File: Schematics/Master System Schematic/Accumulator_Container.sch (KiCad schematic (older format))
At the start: 20 parts, among them J10 Main TS Connector, J11 TSAL Connector, J8 Shutdown/MC Control Connector, J9 TSMP/IMD Connector, K10 SPST-NO (Precharge Control), K11 SPST-NC (Discharge), K12 SPST-NO (AIR Control), K7 SPST-NO (Precharge), K8 SPST-NO (AIR), K9 SPST-NO (AIR), U14 OrionCurrentSens

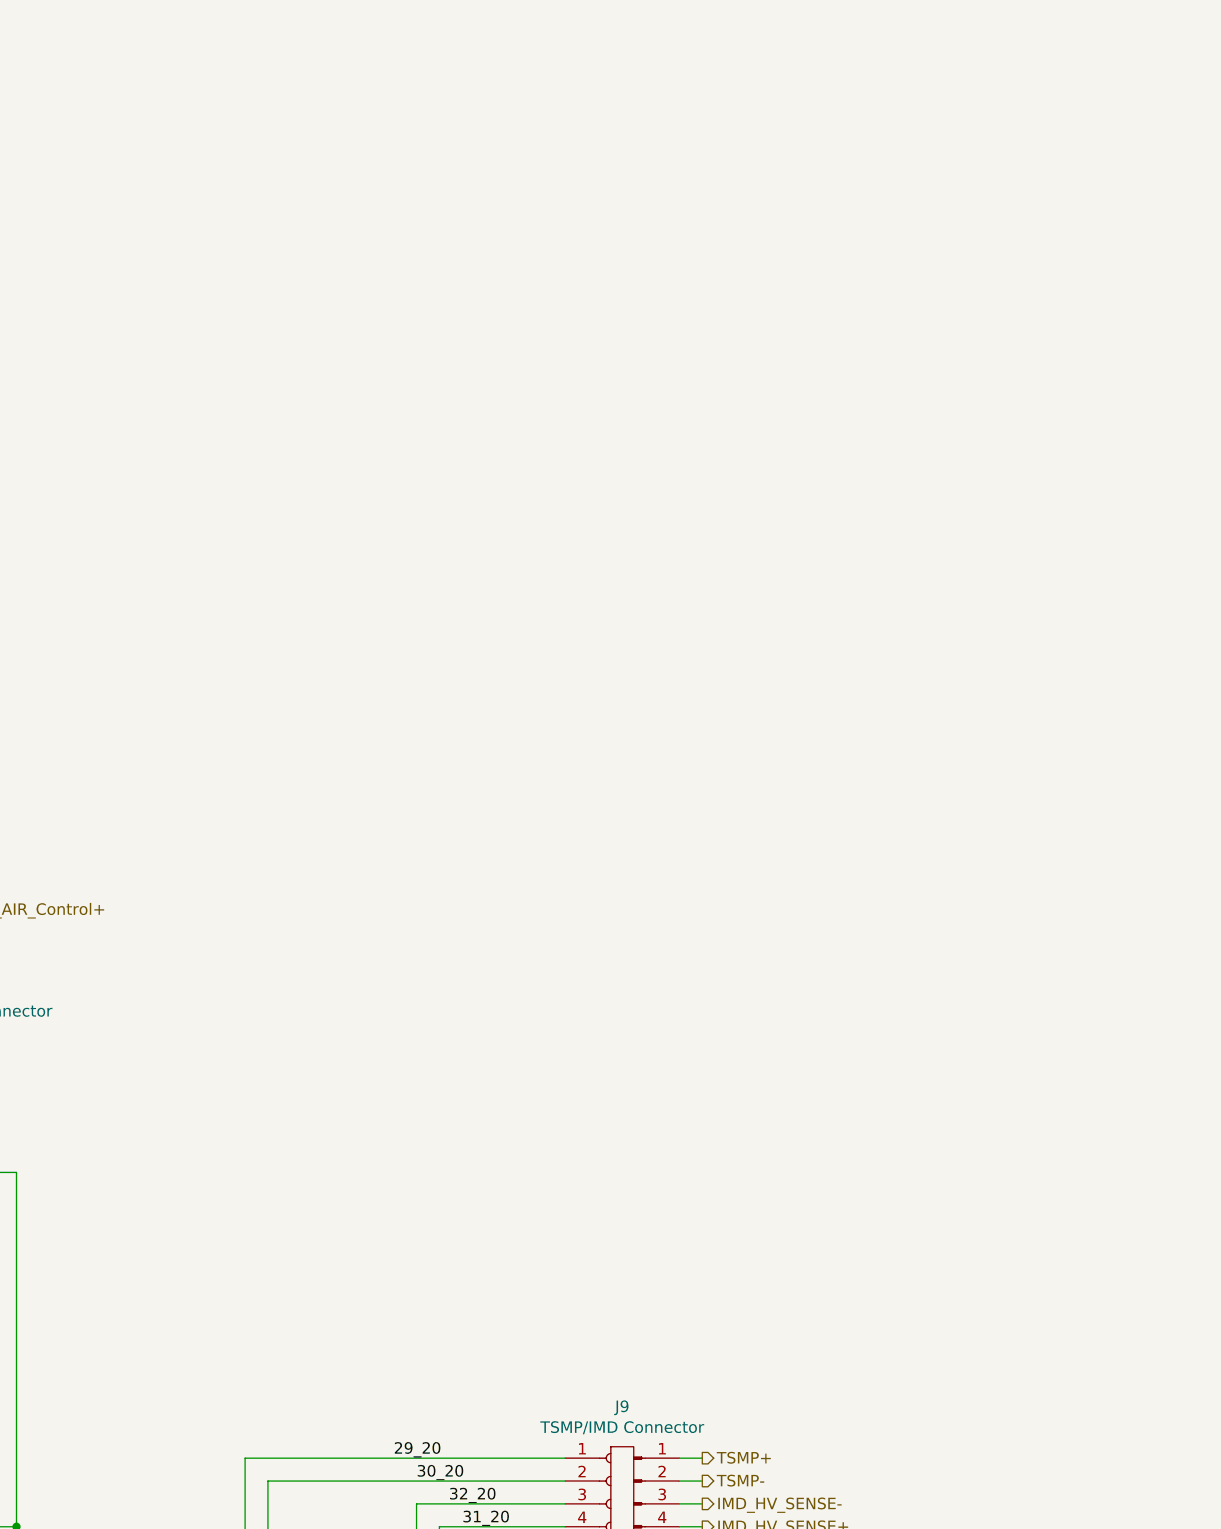
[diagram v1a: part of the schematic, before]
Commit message: Moved Thermistor Exp and MC out of BMS container
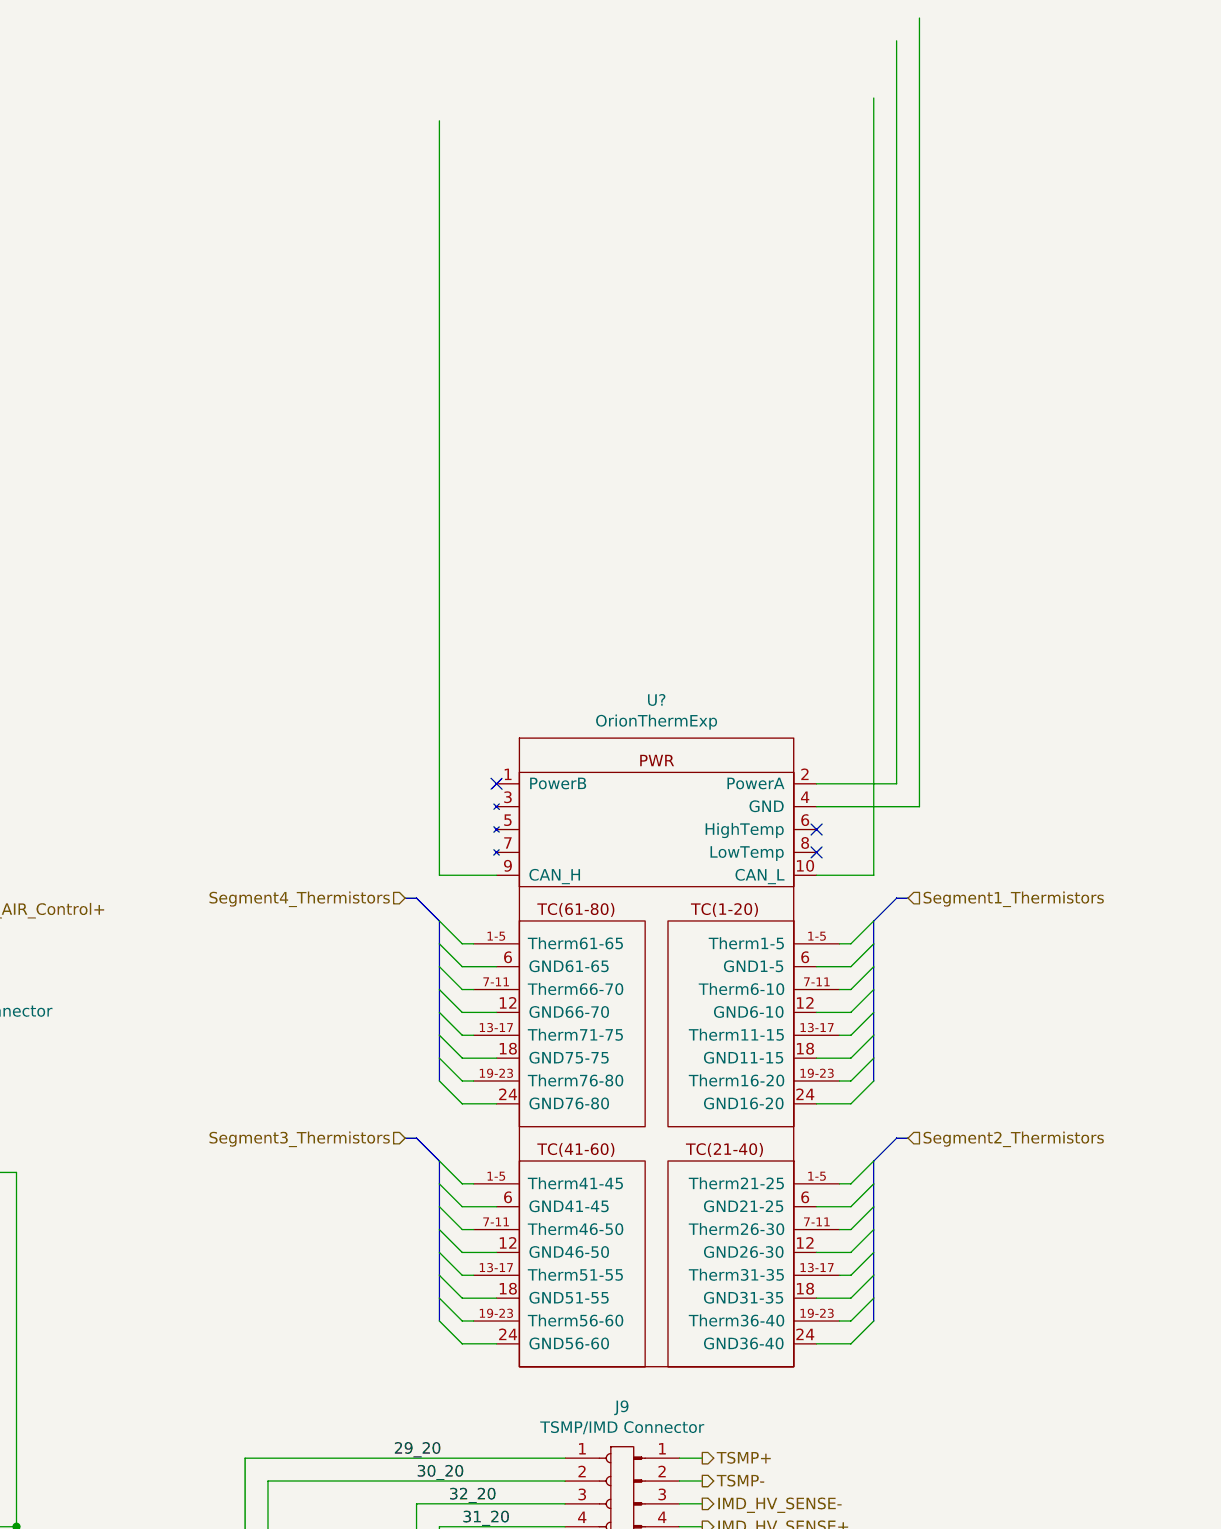
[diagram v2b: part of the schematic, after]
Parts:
- added U?: OrionThermExp, symbol NER:OrionThermExp
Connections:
- no-connect marks 0 -> 3
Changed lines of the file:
@@
 Wire Wire Line
 	9950 600  9950 1050
+Text HLabel 12900 1900 0    50   Input ~ 0
+Segment3_Thermistors
+Text HLabel 15100 850  2    50   Input ~ 0
+Segment1_Thermistors
+Entry Wire Line
+	14850 1750 14950 1650
+Entry Wire Line
+	14850 1650 14950 1550
+Entry Wire Line
+	14850 1550 14950 1450
+Entry Wire Line
+	14850 1450 14950 1350
+Entry Wire Line
+	14850 1350 14950 1250
+Entry Wire Line
+	14850 1250 14950 1150
+Entry Wire Line
+	14850 1150 14950 1050
+Entry Wire Line
+	14850 1050 14950 950
+Entry Bus Bus
+	14950 950  15050 850
+Wire Bus Line
+	15050 850  15100 850
+Entry Wire Line
+	13150 1650 13050 1550
+Entry Wire Line
+	13150 1550 13050 1450
+Entry Wire Line
+	13150 1450 13050 1350
+Entry Wire Line
+	13150 1350 13050 1250
+Entry Wire Line
+	13150 1250 13050 1150
+Entry Wire Line
+	13150 1150 13050 1050
+Entry Wire Line
+	13150 1050 13050 950
+Entry Bus Bus
+	13050 950  12950 850
+Wire Bus Line
+	12950 850  12900 850
+Entry Wire Line
+	13150 2800 13050 2700
+Entry Wire Line
+	13150 2700 13050 2600
+Entry Wire Line
+	13150 2600 13050 2500
+Entry Wire Line
+	13150 2500 13050 2400
+Entry Wire Line
+	13150 2400 13050 2300
+Entry Wire Line
+	13150 2300 13050 2200
+Entry Wire Line
+	13150 2200 13050 2100
+Entry Wire Line
+	13150 2100 13050 2000
+Entry Bus Bus
+	13050 2000 12950 1900
+Wire Bus Line
+	12950 1900 12900 1900
+Entry Wire Line
+	14850 2100 14950 2000
+Entry Wire Line
+	14850 2200 14950 2100
+Entry Wire Line
+	14850 2300 14950 2200
+Entry Wire Line
+	14850 2400 14950 2300
+Entry Wire Line
+	14850 2500 14950 2400
+Entry Wire Line
+	14850 2600 14950 2500
+Entry Wire Line
+	14850 2700 14950 2600
+Entry Wire Line
+	14850 2800 14950 2700
+Text HLabel 15100 1900 2    50   Input ~ 0
+Segment2_Thermistors
+Wire Bus Line
+	15050 1900 15100 1900
+Entry Bus Bus
+	14950 2000 15050 1900
+Text HLabel 12900 850  0    50   Input ~ 0
+Segment4_Thermistors
+Entry Wire Line
+	13150 1750 13050 1650
+Wire Wire Line
+	13150 1050 13200 1050
+Wire Wire Line
+	13150 1150 13300 1150
+Wire Wire Line
+	13150 1250 13200 1250
+Wire Wire Line
+	13150 1350 13300 1350
+Wire Wire Line
+	13200 1450 13150 1450
+Wire Wire Line
+	13150 1550 13300 1550
+Wire Wire Line
+	13150 1650 13200 1650
+Wire Wire Line
+	13150 1750 13300 1750
+Wire Wire Line
+	13200 2100 13150 2100
+Wire Wire Line
+	13150 2200 13300 2200
+Wire Wire Line
+	13150 2300 13200 2300
+Wire Wire Line
+	13150 2400 13300 2400
+Wire Wire Line
+	13150 2500 13200 2500
+Wire Wire Line
+	13150 2600 13300 2600
+Wire Wire Line
+	13150 2700 13200 2700
+Wire Wire Line
+	13150 2800 13300 2800
+Wire Wire Line
+	14850 2100 14800 2100
+Wire Wire Line
+	14850 2200 14700 2200
+Wire Wire Line
+	14850 2300 14800 2300
+Wire Wire Line
+	14700 2400 14850 2400
+Wire Wire Line
+	14800 2500 14850 2500
+Wire Wire Line
+	14700 2600 14850 2600
+Wire Wire Line
+	14850 2700 14800 2700
+Wire Wire Line
+	14700 2800 14850 2800
+Wire Wire Line
+	14700 1750 14850 1750
+Wire Wire Line
+	14850 1650 14800 1650
+Wire Wire Line
+	14850 1550 14700 1550
+Wire Wire Line
+	14850 1450 14800 1450
+Wire Wire Line
+	14850 1350 14700 1350
+Wire Wire Line
+	14850 1250 14800 1250
+Wire Wire Line
+	14850 1150 14700 1150
+Wire Wire Line
+	14800 1050 14850 1050
+NoConn ~ 14700 550
+NoConn ~ 14700 650
+NoConn ~ 13300 350
+$Comp
+L NER:OrionThermExp U?
+U 1 1 5FB81724
+P 14000 150
+F 0 "U?" H 14000 315 50  0000 C CNN
+F 1 "OrionThermExp" H 14000 224 50  0000 C CNN
+F 2 "" H 14000 50  50  0001 C CNN
+F 3 "" H 14000 50  50  0001 C CNN
+	1    14000 150
+	1    0    0    -1
+$EndComp
+Wire Wire Line
+	14700 750  14950 750
+Wire Wire Line
+	13050 750  13300 750
+Wire Wire Line
+	15150 450  14700 450
+Wire Wire Line
+	14700 350  15050 350
+Wire Wire Line
+	13050 -2550 13050 750
+Wire Wire Line
+	14950 -2650 14950 750
+Wire Wire Line
+	15050 -2900 15050 350
+Wire Wire Line
+	15150 -3000 15150 450
 Wire Bus Line
 	5950 9200 5950 9800
@@
 Wire Bus Line
 	13900 5350 15900 5350
+Wire Bus Line
+	14950 950  14950 1650
+Wire Bus Line
+	13050 950  13050 1650
+Wire Bus Line
+	13050 2000 13050 2700
+Wire Bus Line
+	14950 2000 14950 2700
 $EndSCHEMATC

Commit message: added thermistor expansion to Accumulator container
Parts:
- gave numbers to parts that had none: 1
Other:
- note added: "All leave the accumulator container via cord grips"
- note added: "Current sense line will be fed from the accumulator to the BMS via its own connector"
- note removed: "Current sense line will be fed from the accumulator to the BMS via the thermistor connectors, and then split back out within the BMS container. May also be done via a separate connector. TBD"
- moved on the sheet: F5, F6, F7, F8, F9, J10, J11, J8, J9, K10, K11, K12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

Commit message: fixed therm boards
fixed therm board implementation
beginning accumulator redraw
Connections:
- wire segments 372 -> 436
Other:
- moved on the sheet: U7

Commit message: roughly spread out accumulator components, updated therms boards
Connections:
- wire segments 436 -> 438
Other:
- note removed: "Current sense line will be fed from the accumulator to the BMS via its own connector"
- moved on the sheet: F5, F6, F7, F8, F9, J10, J11, J8, J9, K10, K11, K12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

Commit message: Master cleanup
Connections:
- net 1_2: now also F6.1; no longer F6.2
- net TSAL_Circuit/VBATT-: now also F6.2; no longer F6.1
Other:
- moved on the sheet: F6, K11, R3
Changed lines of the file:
@@
 L Relay:MSxx-1Bxx-75 K11
 U 1 1 5E637554
-P 14300 8700
-F 0 "K11" V 13733 8700 50  0000 C CNN
-F 1 "SPST-NC (Discharge)" V 13824 8700 50  0000 C CNN
-F 2 "Relay_THT:Relay_SPST_StandexMeder_MS_Form1AB" H 14650 8650 50  0001 L CNN
-F 3 "https://standexelectronics.com/de/produkte/ms-reed-relais/" H 14300 8700 50  0001 C CNN
-	1    14300 8700
+P 14500 10450
+F 0 "K11" V 13933 10450 50  0000 C CNN
+F 1 "SPST-NC (Discharge)" V 14024 10450 50  0000 C CNN
+F 2 "Relay_THT:Relay_SPST_StandexMeder_MS_Form1AB" H 14850 10400 50  0001 L CNN
+F 3 "https://standexelectronics.com/de/produkte/ms-reed-relais/" H 14500 10450 50  0001 C CNN
+	1    14500 10450
 	0    1    1    0
 $EndComp
@@
 Connection ~ 12850 7500
 Wire Wire Line
-	12850 7500 12850 8500
-Wire Wire Line
-	14000 8500 12850 8500
+	14200 10250 12850 10250
 Wire Wire Line
 	13750 6500 13850 6500
-Wire Wire Line
-	13950 8900 14000 8900
 $Comp
 L Device:R R3
 U 1 1 5F158D54
-P 15950 8300
-F 0 "R3" H 15750 8350 50  0000 L CNN
-F 1 "3.3k" H 15700 8250 50  0000 L CNN
-F 2 "" V 15880 8300 50  0001 C CNN
-F 3 "~" H 15950 8300 50  0001 C CNN
-	1    15950 8300
+P 15950 9250
+F 0 "R3" H 15750 9300 50  0000 L CNN
+F 1 "3.3k" H 15700 9200 50  0000 L CNN
+F 2 "" V 15880 9250 50  0001 C CNN
+F 3 "~" H 15950 9250 50  0001 C CNN
+	1    15950 9250
 	1    0    0    -1
 $EndComp
@@
 Text Label 15450 4400 0    50   ~ 0
 26_20
-Text Label 14800 8900 0    50   ~ 0
+Text Label 15000 10650 0    50   ~ 0
 13_2
 Text Label 13850 4250 2    50   ~ 0
@@
 	15100 3150 15200 3150
 Wire Wire Line
-	14600 8500 15450 8500
+	14800 10250 15450 10250
 Wire Wire Line
 	14250 3900 15200 3900
@@
 	15950 7900 16450 7900
 Wire Wire Line
-	15950 8150 15950 7900
-Wire Wire Line
-	15950 8450 15950 8900
-Wire Wire Line
-	14600 8900 15950 8900
+	15950 9100 15950 7900
+Wire Wire Line
+	14800 10650 15950 10650
 $Comp
 L NER:2-Pos_Generic J10
@@
 Wire Wire Line
 	2350 2200 2650 2200
-Wire Wire Line
-	11750 13850 13150 13850
-Wire Wire Line
-	11750 14300 11750 14400
 $Comp
 L Device:Fuse F6
 U 1 1 5FC95B82
-P 11750 14150
-F 0 "F6" H 11691 14104 50  0000 R CNN
-F 1 "Fuse" H 11691 14195 50  0000 R CNN
-F 2 "" V 11680 14150 50  0001 C CNN
-F 3 "~" H 11750 14150 50  0001 C CNN
-	1    11750 14150
+P 11850 13450
+F 0 "F6" H 11791 13404 50  0000 R CNN
+F 1 "Fuse" H 11791 13495 50  0000 R CNN
+F 2 "" V 11780 13450 50  0001 C CNN
+F 3 "~" H 11850 13450 50  0001 C CNN
+	1    11850 13450
 	1    0    0    1
 $EndComp
-Wire Wire Line
-	17700 14400 11750 14400
-Wire Wire Line
-	17600 14300 11850 14300
 Wire Wire Line
 	16550 8350 16550 13850
@@
 $EndComp
 Wire Wire Line
-	5250 13850 11750 13850
-Connection ~ 11750 13850
-Wire Wire Line
-	11750 13850 11750 14000
+	11850 11950 11850 13300
 Wire Wire Line
 	5250 13750 6100 13750
 Wire Wire Line
-	11850 7450 11850 14300
+	11850 7450 11850 11850
 Connection ~ 16550 8350
 Wire Wire Line
@@
 	17300 7900 17850 7900
 Wire Wire Line
-	17600 6350 17600 14300
-Wire Wire Line
-	17700 14400 17700 6450
-Connection ~ 12850 8500
-Wire Wire Line
-	12850 8500 12850 13450
-Wire Wire Line
-	15450 8500 15450 13450
-Wire Wire Line
-	13750 13850 13950 13850
-Wire Wire Line
-	13950 13850 16550 13850
-Connection ~ 13950 13850
-Wire Wire Line
-	13950 8900 13950 13850
+	17600 6350 17600 11850
 Wire Wire Line
 	13750 6900 15950 6900
-Wire Wire Line
-	15450 3900 15450 8500
 Connection ~ 15450 3900
-Connection ~ 15450 8500
 Wire Wire Line
 	14400 3550 14400 7500
@@
 	17100 15000 19650 15000
 Wire Bus Line
-	20150 7250 20150 12000
+	20700 7250 20700 12000
 Wire Bus Line
 	19250 13700 19650 13700
@@
 	20850 750  20850 12150
 Wire Bus Line
-	19100 12000 20150 12000
+	19100 12000 20700 12000
+Wire Bus Line
+	19250 12150 20850 12150
+Wire Wire Line
+	13750 13850 14000 13850
+Connection ~ 12850 10250
+Wire Wire Line
+	12850 10250 12850 13450
+Connection ~ 15450 10250
+Wire Wire Line
+	15450 10250 15450 13450
+Wire Wire Line
+	12850 7500 12850 10250
+Wire Wire Line
+	15450 3900 15450 10250
+Wire Wire Line
+	14200 10650 14000 10650
+Wire Wire Line
+	14000 10650 14000 13850
+Connection ~ 14000 13850
+Wire Wire Line
+	14000 13850 16550 13850
+Wire Wire Line
+	15950 9400 15950 10650
+Wire Wire Line
+	17700 11950 17700 6450
+Wire Wire Line
+	5250 13850 11850 13850
+Wire Wire Line
+	11850 13600 11850 13850
+Connection ~ 11850 13850
+Wire Wire Line
+	11850 13850 13150 13850
+Wire Wire Line
+	17700 11950 11850 11950
+Wire Wire Line
+	17600 11850 11850 11850
 Wire Bus Line
 	10550 14800 10550 15000
 Wire Bus Line
+	10600 12200 10600 14750
+Wire Bus Line
+	10650 9300 10650 14700
+Wire Bus Line
+	10700 6400 10700 14650
+Wire Bus Line
 	2650 750  20850 750
 Wire Bus Line
-	10650 9300 10650 14700
-Wire Bus Line
-	10700 6400 10700 14650
-Wire Bus Line
-	10600 12200 10600 14750
-Wire Bus Line
 	2550 850  2550 1800
 Wire Bus Line
-	18150 7250 20150 7250
-Wire Bus Line
 	4400 3350 4400 4400
 Wire Bus Line
@@
 	2250 2300 2250 4300
 Wire Bus Line
-	19250 12150 20850 12150
+	18150 7250 20700 7250
 $EndSCHEMATC

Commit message: Finished master and accum cleanup
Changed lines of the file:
@@
 Sheet 4 22
 Title "Accumulator Container"
-Date "2020-11-11"
-Rev "5"
+Date "2020-11-12"
+Rev "6"
 Comp "Northeastern Electric Racing"
 Comment1 "https://github.com/Northeastern-Electric-Racing/NER"
@@
 NoConn ~ 2750 1800
 NoConn ~ 4150 1500
-Text HLabel 19650 14900 2    50   Output ~ 0
+Text HLabel 19650 14850 2    50   Output ~ 0
 Segment1_CriticalThermistors
-Text HLabel 19650 15000 2    50   Output ~ 0
+Text HLabel 19650 14950 2    50   Output ~ 0
 Segment2_CriticalThermistors
-Text HLabel 19650 15100 2    50   Output ~ 0
+Text HLabel 19650 15050 2    50   Output ~ 0
 Segment3_CriticalThermistors
-Text HLabel 19650 15200 2    50   Output ~ 0
+Text HLabel 19650 15150 2    50   Output ~ 0
 Segment4_CriticalThermistors
 Entry Wire Line
@@
 	1300 8050 650  8050
 Wire Bus Line
-	650  8050 650  16350
+	650  8050 650  16300
 Wire Bus Line
 	1300 10950 700  10950
@@
 	1300 13850 750  13850
 Wire Bus Line
-	750  13850 750  16250
-Wire Bus Line
-	700  10950 700  16300
+	750  13850 750  16100
+Wire Bus Line
+	700  10950 700  16200
 Wire Bus Line
 	1300 13750 800  13750
@@
 	10100 2150 10100 5600
 Wire Bus Line
-	17200 16400 17200 15200
-Wire Bus Line
-	600  16400 17200 16400
-Wire Bus Line
-	17150 16350 17150 15100
-Wire Bus Line
-	650  16350 17150 16350
-Wire Bus Line
-	17100 16300 17100 15000
-Wire Bus Line
-	700  16300 17100 16300
-Wire Bus Line
-	750  16250 17050 16250
-Wire Bus Line
-	17100 15000 19650 15000
+	13650 16400 13650 15150
+Wire Bus Line
+	600  16400 13650 16400
+Wire Bus Line
+	13550 16300 13550 15050
+Wire Bus Line
+	650  16300 13550 16300
+Wire Bus Line
+	13450 16200 13450 14950
+Wire Bus Line
+	700  16200 13450 16200
+Wire Bus Line
+	750  16100 13350 16100
+Wire Bus Line
+	13450 14950 19650 14950
 Wire Bus Line
 	20700 7250 20700 12000
@@
 	10500 12200 10600 12300
 Wire Bus Line
-	8050 15000 10450 15000
-Wire Bus Line
-	8050 15100 10450 15100
+	8050 15000 10500 15000
+Wire Bus Line
+	8050 15100 10500 15100
 Entry Bus Bus
-	10450 15100 10550 15000
+	10500 15100 10600 15000
 Entry Bus Bus
-	10450 15000 10550 14900
+	10500 15000 10600 14900
 Wire Bus Line
 	8050 6400 10600 6400
 Wire Bus Line
 	8050 6300 10600 6300
-Wire Bus Line
-	18750 14550 19650 14550
-Wire Bus Line
-	18700 14450 19650 14450
-Wire Bus Line
-	18650 14350 19650 14350
-Wire Bus Line
-	19650 14250 18600 14250
-Wire Bus Line
-	10700 14650 18600 14650
-Wire Bus Line
-	10650 14700 18650 14700
-Wire Bus Line
-	18600 14250 18600 14650
 Wire Notes Line
 	21100 15250 21100 13600
 Wire Bus Line
-	17200 15200 19650 15200
-Wire Bus Line
-	18650 14700 18650 14350
-Wire Bus Line
-	18700 14750 18700 14450
-Wire Bus Line
-	18750 14800 18750 14550
-Wire Bus Line
-	17050 14900 19650 14900
-Wire Bus Line
-	17050 14900 17050 16250
-Wire Bus Line
-	17150 15100 19650 15100
+	13650 15150 19650 15150
+Wire Bus Line
+	13550 15050 19650 15050
 Wire Notes Line
 	19450 13600 19450 15250
 Wire Bus Line
-	10600 14750 18700 14750
-Wire Bus Line
-	10550 14800 18750 14800
-Wire Bus Line
 	19100 12000 19100 14000
 Wire Bus Line
@@
 	17600 11850 11850 11850
 Wire Bus Line
-	10550 14800 10550 15000
-Wire Bus Line
-	10600 12200 10600 14750
-Wire Bus Line
-	10650 9300 10650 14700
-Wire Bus Line
-	10700 6400 10700 14650
+	10700 14250 19650 14250
+Wire Bus Line
+	10650 14350 19650 14350
+Wire Bus Line
+	10600 14450 19650 14450
+Wire Bus Line
+	10600 14550 19650 14550
+Wire Bus Line
+	13350 14850 13350 16100
+Wire Bus Line
+	13350 14850 19650 14850
+Wire Bus Line
+	10600 14550 10600 15000
+Wire Bus Line
+	10600 12200 10600 14450
+Wire Bus Line
+	10650 9300 10650 14350
+Wire Bus Line
+	10700 6400 10700 14250
 Wire Bus Line
 	2650 750  20850 750
@@
 	2550 850  2550 1800
 Wire Bus Line
+	18150 7250 20700 7250
+Wire Bus Line
 	4400 3350 4400 4400
 Wire Bus Line
@@
 Wire Bus Line
 	2250 2300 2250 4300
-Wire Bus Line
-	18150 7250 20700 7250
 $EndSCHEMATC
